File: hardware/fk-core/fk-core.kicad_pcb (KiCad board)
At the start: 2 copper layers, 0 parts

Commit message: MUP based board is the primary board now.
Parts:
- added C1: 18pF, RocketScreamKicadLibrary:CAP-0402, F.Cu at (139.2, 81.3)
- added C10: 4.7uF 10V X5R, RocketScreamKicadLibrary:CAP-0402, F.Cu at (139.4, 117.3)
- added C11: 4.7uF 10V X5R, RocketScreamKicadLibrary:CAP-0402, F.Cu at (139.4, 77.7)
- added C12: 100nF, RocketScreamKicadLibrary:CAP-0402, F.Cu at (139.4, 76.5)
- added C13: 100nF, RocketScreamKicadLibrary:CAP-0402, F.Cu at (132.6, 102.6)
- added C14: 4.7uF 10V X5R, RocketScreamKicadLibrary:CAP-0402, F.Cu at (133.7, 85.3)
- added C15: 1uF 10V X5R, RocketScreamKicadLibrary:CAP-0402, F.Cu at (139.2, 109.0)
- added C16: 4.7uF 10V X5R, RocketScreamKicadLibrary:CAP-0402, F.Cu at (136.4, 116.6)
- added C17: 4.7uF 10V X5R, RocketScreamKicadLibrary:CAP-0402, F.Cu at (137.7, 109.0)
- added C18: 4.7nF 25V X7R, RocketScreamKicadLibrary:CAP-0402, F.Cu at (145.8, 135.0)
- added C19: 1uF 10V X5R, RocketScreamKicadLibrary:CAP-0402, F.Cu at (140.0, 104.6)
- added C2: 18pF, RocketScreamKicadLibrary:CAP-0402, F.Cu at (141.2, 83.3)
- added C20: 1uF 10V X5R, RocketScreamKicadLibrary:CAP-0603, F.Cu at (143.1, 119.2)
- added C3: 100nF, RocketScreamKicadLibrary:CAP-0402, F.Cu at (145.0, 84.8)
- added C4: 100nF, RocketScreamKicadLibrary:CAP-0402, F.Cu at (132.5, 85.9)
- added C5: 1uF 10V X5R, RocketScreamKicadLibrary:CAP-0402, F.Cu at (146.3, 84.8)
- added C6: 100nF, RocketScreamKicadLibrary:CAP-0402, F.Cu at (135.0, 85.3)
- added C7: 100nF, RocketScreamKicadLibrary:CAP-0402, F.Cu at (147.3, 93.4)
- added C8: 100nF, RocketScreamKicadLibrary:CAP-0402, F.Cu at (131.6, 95.5)
- added C9: 1uF 50V X5R, RocketScreamKicadLibrary:CAP-0603, F.Cu at (134.1, 109.0)
- added D1: Orange, RocketScreamKicadLibrary:LED-0603, F.Cu at (144.5, 102.9)
- added D2: LED-DUAL, RocketScreamKicadLibrary:LED-1615, F.Cu at (144.5, 112.1)
- added D3: PRTR5V0U2X, RocketScreamKicadLibrary:SOT-143B, F.Cu at (148.0, 125.8)
- added D4: PMEG3020CPA, RocketScreamKicadLibrary:SOT-1016, F.Cu at (131.8, 110.7)
- added D5: Red, RocketScreamKicadLibrary:LED-0603, F.Cu at (131.4, 60.1)
- added F1: MF-PSMF050X-2, RocketScreamKicadLibrary:MF-PSMF020X, F.Cu at (138.2, 121.4)
- added G***: LOGO, logos:conservify_normal_3500, F.Cu at (134.1, 135.0)
- added G***: LOGO, logos:ngfk_normal_3500, F.Cu at (129.7, 139.8)
- added G***: LOGO, logos:osh_normal_3000, F.Cu at (137.8, 135.0)
- added J1: S2B-PH-SM4-TB, RocketScreamKicadLibrary:S2B-PH-SM4-TB, F.Cu at (131.6, 128.7)
- added J2: MICRO-USB, RocketScreamKicadLibrary:MICRO-USB, F.Cu at (149.9, 132.4)
- added J3: RF-SMA-EDGE, RocketScreamKicadLibrary:RF-SMA-EDGE, F.Cu at (129.0, 69.9)
- added J4: CONN-HDR-1x19, RocketScreamKicadLibrary:HDR_1x19_Pitch2.54mm_WithoutSilk, F.Cu at (128.3, 99.1)
- added J5: CONN-HDR-1x19, RocketScreamKicadLibrary:HDR_1x19_Pitch2.54mm_WithoutSilk, F.Cu at (151.1, 99.1)
- added J6: CONN-HDR-2x5, RocketScreamKicadLibrary:HDR_2x5_Pitch1.27mm, F.Cu at (145.0, 76.6)
- added J7: RF-SMA-EDGE, RocketScreamKicadLibrary:RF-SMA-EDGE, F.Cu at (143.8, 50.0)
- added L1: BKP1005TS121-T, RocketScreamKicadLibrary:IND-0402, F.Cu at (140.7, 117.3)
- added L2: BKP1005TS121-T, RocketScreamKicadLibrary:IND-0402, F.Cu at (131.2, 85.9)
- added M1: MOUNT_HOLE, RocketScreamKicadLibrary:HOLE_NPTH_2.2MM, F.Cu at (128.4, 151.6)
- added M2: MOUNT_HOLE, RocketScreamKicadLibrary:HOLE_NPTH_2.2MM, F.Cu at (151.2, 151.5)
- added M3: MOUNT_HOLE, RocketScreamKicadLibrary:HOLE_NPTH_2.2MM, F.Cu at (128.4, 49.4)
- added M4: MOUNT_HOLE, RocketScreamKicadLibrary:HOLE_NPTH_2.2MM, F.Cu at (151.2, 49.4)
- added M7: MICROSD, microsd:MICROSD, F.Cu at (132.5, 137.5)
- added P1: CONN-HDR-MODULE, fk-core-mini-ultra-pro:Socket_Strip_Straight_1x05_Pitch2.54mm, F.Cu at (151.1, 148.6)
- added Q1: 2N7002LT1G, RocketScreamKicadLibrary:SOT-23, F.Cu at (141.0, 101.3)
- added R1: 2K2, RocketScreamKicadLibrary:RES-0402, F.Cu at (144.5, 101.3)
- added R10: 2K2, RocketScreamKicadLibrary:RES-0402, F.Cu at (132.1, 115.6)
- added R11: 100K, RocketScreamKicadLibrary:RES-0402, F.Cu at (147.3, 91.2)
- added R12: 10K, RocketScreamKicadLibrary:RES-0402, F.Cu at (142.0, 112.8)
- added R13: 2K2, RocketScreamKicadLibrary:RES-0402, F.Cu at (142.0, 111.5)
- added R14: 1k, RocketScreamKicadLibrary:RES-0603, F.Cu at (141.3, 121.0)
- added R15: 180, RocketScreamKicadLibrary:RES-0603, F.Cu at (143.1, 122.8)
- added R16: 470R, RocketScreamKicadLibrary:RES-0603, F.Cu at (131.4, 56.5)
- added R17: 4.7K, RocketScreamKicadLibrary:RES-0603, F.Cu at (145.8, 114.8)
- added R18: 4.7K, RocketScreamKicadLibrary:RES-0603, F.Cu at (145.8, 116.5)
- added R2: 330R, RocketScreamKicadLibrary:RES-0402, F.Cu at (145.8, 80.0)
- added R3: 330R, RocketScreamKicadLibrary:RES-0402, F.Cu at (147.3, 89.9)
- added R4: 10K, RocketScreamKicadLibrary:RES-0402, F.Cu at (144.5, 80.0)
- added R5: 1M, RocketScreamKicadLibrary:RES-0402, F.Cu at (145.8, 136.5)
- added R6: 1K18, RocketScreamKicadLibrary:RES-0402, F.Cu at (135.9, 109.0)
- added R7: 46K4, RocketScreamKicadLibrary:RES-0402, F.Cu at (132.1, 113.0)
- added R8: 10K, RocketScreamKicadLibrary:RES-0402, F.Cu at (132.1, 116.8)
- added R9: 2K94, RocketScreamKicadLibrary:RES-0402, F.Cu at (132.1, 114.3)
- added SW1: SPNO, RocketScreamKicadLibrary:TS-018, F.Cu at (151.7, 54.9)
- added U1: ATSAMD21G18A-AU, RocketScreamKicadLibrary:TQFP-48_7x7mm_Pitch0.5mm, F.Cu at (139.7, 91.4)
- added U2: BQ24074RGTT, RocketScreamKicadLibrary:QFN-16_3x3mm, F.Cu at (137.0, 113.0)
- added U3: RFM95W, RocketScreamKicadLibrary:RFM9xW, B.Cu at (139.7, 87.6)
- added U4: MCP1700T-3302E/MB, RocketScreamKicadLibrary:SOT-89, F.Cu at (143.3, 107.4)
- added U5: S25FL116K0XMFI041, RocketScreamKicadLibrary:SOIC-8-N, F.Cu at (136.1, 102.6)
- added U6: MAX1704XX, Housings_DFN_QFN:DFN-8-1EP_2x2mm_Pitch0.5mm, F.Cu at (145.5, 120.9)
- added U7: FGPMMOPA6H, FGPMMOPA6H:FGPMMOPA6H, B.Cu at (141.8, 62.2)
- added Y1: FC-135, RocketScreamKicadLibrary:ABS07, F.Cu at (138.9, 83.6)
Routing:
- net 3V3: track 0.00 -> 210.9 mm, vias 0 -> 19
- net /MISO: track 0.00 -> 96.4 mm, vias 0 -> 3
- net /SCK: track 0.00 -> 82.3 mm, vias 0 -> 4
- net /MOSI: track 0.00 -> 81.6 mm, vias 0 -> 4
- net GND: track 0.00 -> 69.4 mm, vias 0 -> 43
- net /D13: track 0.00 -> 68.8 mm, vias 0 -> 2
- net /D1: track 0.00 -> 67.1 mm, vias 0 -> 1
- net /D0: track 0.00 -> 65.0 mm, vias 0 -> 1
- net /SCL: track 0.00 -> 60.2 mm, vias 0 -> 1
- net /SDA: track 0.00 -> 57.5 mm, vias 0 -> 1
- net VBAT: track 0.00 -> 54.9 mm
- net Net-(J2-Pad4): track 0.00 -> 45.5 mm
- net /USB-: track 0.00 -> 45.4 mm
- net /USB+: track 0.00 -> 44.8 mm
- net /A1: track 0.00 -> 40.9 mm, vias 0 -> 1
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- added copper zone on B.Cu, net 3V3
- added copper zone on F.Cu, net 3V3
- added copper zone on B.Cu, net 5V0
- added copper zone on F.Cu, net 5V0
- added copper zone on B.Cu, net GND
- added copper zone on F.Cu, net GND
- added copper zone on F.Cu, net VBAT
- added copper zone on B.Cu, net VBUS
- added copper zone on F.Cu, net VBUS
- added copper zone on F.Cu, net VEXT
- added copper zone on F.Cu, net VIN
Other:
- board outline added: 26.2 x 105.4 mm
- net class Default: trace_width 0.1524 -> 0.254; via_dia 0.6858 -> 0.5; via_drill 0.3302 -> 0.3
- net class RF-50Ohm added: clearance 0.254, trace_width 1.27, via_dia 0.5, via_drill 0.3
- rule pad_to_mask_clearance: 0.2 -> 0.1016
- rule trace_min: 0.1524 -> 0.19
- rule via_min_drill: 0.3302 -> 0.3
- rule via_min_size: 0.6858 -> 0.4
- board text added: "0"
- board text added: "1"
- board text added: "10"
- board text added: "11"
- board text added: "12"
- board text added: "13"
- board text added: "2"
- board text added: "3"
- board text added: "30"
- board text added: "31"
- board text added: "3V3"
- board text added: "4"
- board text added: "5"
- board text added: "5V"
- board text added: "6"
- board text added: "7"
- board text added: "8"
- board text added: "9"
- board text added: "A0"
- board text added: "A1"
- board text added: "A2"
- board text added: "A3"
- board text added: "A4"
- board text added: "A5"
- board text added: "AREF"
- board text added: "ATN"
- board text added: "BAT"
- board text added: "CHG"
- board text added: "GND"
- board text added: "LED-D13"
- board text added: "MISO"
- board text added: "MOSI"
- board text added: "PG"
- board text added: "PWM"
- board text added: "RST"
- board text added: "SCK"
- board text added: "SCL"
- board text added: "SDA"
- board text added: "SWD"
- board text added: "Serial"
- board text added: "Serial1"
- board text added: "VBUS"
- board text added: "VIN"
- board text added: "VIN:5-10.5V"
- board text added: "v0.1"

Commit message: Incorporating suggestions from Dave.
* SW1 is awfully close to the RF connection on U7. Can this slide south? Pins 15/15/17/18 are all no connect, having a switch close to that would be easier.
* If you move J7 to the other side of the board, then we won't need a via in the middle of the RF transmission line there.
* R16 is sized to bias A1 at about 3 mA. the default is to toggle on/off when it's locking, then go low when the system is locked. Bumping R16 to ~ 1Kohm will half the current, which might be enough for a high brightness LED.
Done! Thanks!

* Could J3 get flipped so that the RF path stays on the bottom, instead of running through a Via?
Done! I had to narrow and get creative with the A1 trace to route around this, hopefully that's ok.

* Vbackup on U7 might be worthwhile to hookup. the current consumption is pretty low (7 uA) and will let the GPS lock faster when power is applied.
I'll look into doing this. I'm just worried about getting VBAT over to that end of the board, haha.

* If you rotate C1/C2 180 degrees, you can ground both of them at the same via/Ground node.
Good call, where would you put the new via? There's a tight fit right there with the 3v3 to the radio and the edge of the bottom GND fill.

* J1 is an SMT part. Is there one available with through hole mounting pins so the connector doesn't rip off the board?
Good idea, I'll dig around and see if we can find one.

* The BQ24074 supports temp sensing on the battery pack, but the JST connector only has Batt+ and GND. Did you set the charging current on the low side?
* The RFM95 sits right underneath the 32kHz Clock crystal for the SAMD21. The 32kHz is a fairly strong oscillator (32kHz Square wave that goes 0 to 3.3V) and I'm worried that it will couple directly into the RF output of the RFM95 through the Power supply or directly radiated through the board. A 4 layer board with full ground planes would help significantly.

We based our board on an already designed and produced one and these a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
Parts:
- added M5, M6: FIDUCIAL, RocketScreamKicadLibrary:FIDUCIAL-1MM, F.Cu at (139.9, 163.3)
- J3, J7: moved to B.Cu
- R16: value 470R -> 1k
- moved SW1 16.3 mm to (151.7, 71.2)
- turned C1 to 135 degrees
- turned C2 to 315 degrees
- turned J7 to 270 degrees
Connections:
- U7 pad 4: (no net) -> VBAT
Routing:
- net VBAT: track 54.9 -> 114.1 mm, vias 0 -> 1
- net /RST: track 31.0 -> 14.7 mm
- net GND: track 69.4 -> 76.0 mm, vias 43 -> 45
- net /A1: track 40.9 -> 42.2 mm
- net Net-(C1-Pad2): track 6.68 -> 7.73 mm
- net Net-(C2-Pad2): track 5.61 -> 6.66 mm
- net 3V3: track 210.9 -> 209.9 mm, vias 19 -> 18
- net Net-(J3-Pad1): track 13.2 -> 13.7 mm, vias 1 -> 0
- net Net-(J7-Pad1): vias 2 -> 0

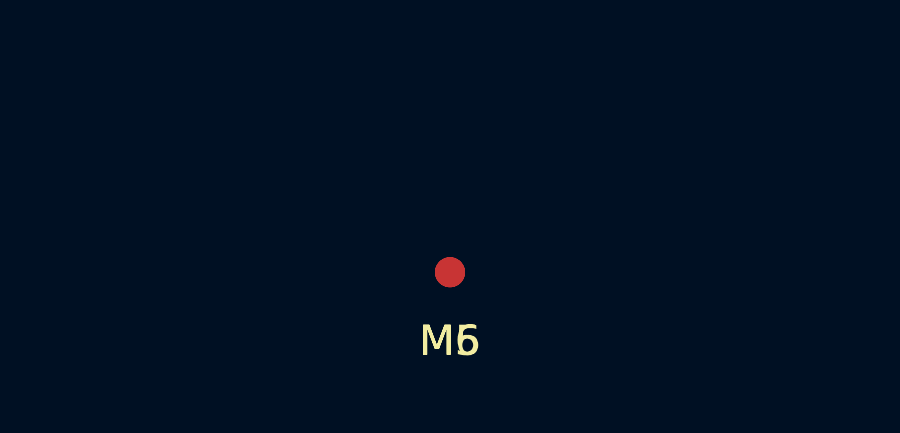
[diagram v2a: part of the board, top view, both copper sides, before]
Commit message: Remove fudicial for now.
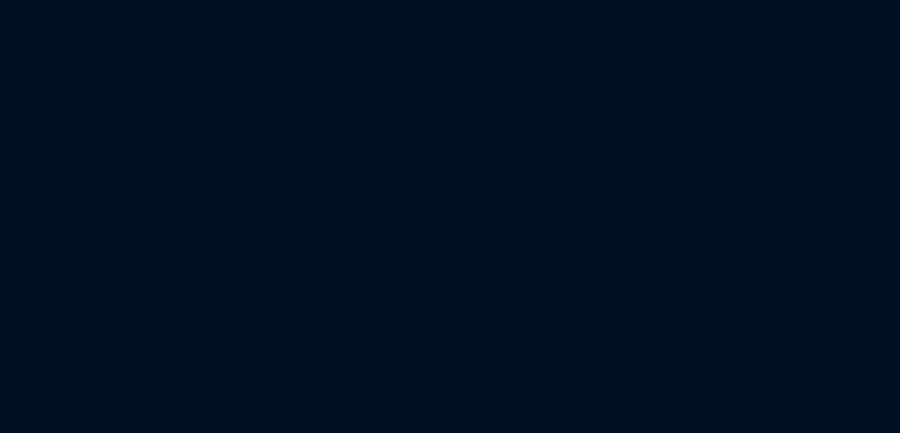
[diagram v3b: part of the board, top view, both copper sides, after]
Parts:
- removed M5, M6: FIDUCIAL, RocketScreamKicadLibrary:FIDUCIAL-1MM
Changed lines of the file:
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@@
   (general
     (links 220)
-    (no_connects 0)
-    (area 126.724999 47.724999 153.075001 153.275001)
+    (no_connects 77)
+    (area 104.521 44.198381 174.451 166.690001)
     (thickness 1.6)
     (drawings 86)
     (tracks 1006)
     (zones 0)
-    (modules 74)
+    (modules 72)
     (nets 68)
   )
@@
   )
   (setup
-    (last_trace_width 0.2032)
+    (last_trace_width 0.254)
     (user_trace_width 0.2032)
     (user_trace_width 0.254)
@@
       (xy 1.374306 0.851583) (xy 1.397389 0.846667) (xy 1.419502 0.853764)) (layer F.SilkS) (width 0.01))
   )
-  (module RocketScreamKicadLibrary:FIDUCIAL-1MM (layer F.Cu)
-    (at 139.9 163.275001)
-    (descr "Circular Fiducial, 1mm bare copper top; 2.54mm keepout")
-    (tags marker)
-    (attr virtual)
-    (fp_text reference M5 (at 0 2.286) (layer F.SilkS)
-      (effects (font (size 1 1) (thickness 0.15)))
-    )
-    (fp_text value FIDUCIAL (at 0 -2.032) (layer F.Fab)
-      (effects (font (size 1 1) (thickness 0.15)))
-    )
-    (pad ~ smd circle (at 0 0) (size 1 1) (layers F.Cu F.Mask)
-      (solder_mask_margin 0.5) (clearance 0.5))
-  )
-  (module RocketScreamKicadLibrary:FIDUCIAL-1MM (layer F.Cu)
-    (at 139.9 163.275001)
-    (descr "Circular Fiducial, 1mm bare copper top; 2.54mm keepout")
-    (tags marker)
-    (attr virtual)
-    (fp_text reference M6 (at 0 2.286) (layer F.SilkS)
-      (effects (font (size 1 1) (thickness 0.15)))
-    )
-    (fp_text value FIDUCIAL (at 0 -2.032) (layer F.Fab)
-      (effects (font (size 1 1) (thickness 0.15)))
-    )
-    (pad ~ smd circle (at 0 0) (size 1 1) (layers F.Cu F.Mask)
-      (solder_mask_margin 0.5) (clearance 0.5))
-  )
   (gr_text v0.1 (at 128.52 147.25) (layer F.SilkS)
     (effects (font (size 0.8 0.8) (thickness 0.15)))
@@
     (connect_pads (clearance 0.2032))
     (min_thickness 0.2032)
-    (fill (arc_segments 32) (thermal_gap 0.254) (thermal_bridge_width 0.254) (smoothing chamfer))
+    (fill yes (arc_segments 32) (thermal_gap 0.254) (thermal_bridge_width 0.254) (smoothing chamfer))
     (polygon
       (pts
@@
     (connect_pads (clearance 0.2032))
     (min_thickness 0.2032)
-    (fill (arc_segments 32) (thermal_gap 0.254) (thermal_bridge_width 0.254) (smoothing chamfer))
+    (fill yes (arc_segments 32) (thermal_gap 0.254) (thermal_bridge_width 0.254) (smoothing chamfer))
     (polygon
       (pts
@@
     (connect_pads (clearance 0.2032))
     (min_thickness 0.253)
-    (fill (arc_segments 32) (thermal_gap 0.254) (thermal_bridge_width 0.254) (smoothing chamfer))
+    (fill yes (arc_segments 32) (thermal_gap 0.254) (thermal_bridge_width 0.254) (smoothing chamfer))
     (polygon
       (pts
@@
     (connect_pads (clearance 0.2032))
     (min_thickness 0.2032)
-    (fill (arc_segments 32) (thermal_gap 0.254) (thermal_bridge_width 0.254) (smoothing chamfer))
+    (fill yes (arc_segments 32) (thermal_gap 0.254) (thermal_bridge_width 0.254) (smoothing chamfer))
     (polygon
       (pts
@@
     (connect_pads (clearance 0.2032))
     (min_thickness 0.253)
-    (fill (arc_segments 32) (thermal_gap 0.254) (thermal_bridge_width 0.254) (smoothing chamfer))
+    (fill yes (arc_segments 32) (thermal_gap 0.254) (thermal_bridge_width 0.254) (smoothing chamfer))
     (polygon
       (pts
@@
     (connect_pads (clearance 0.254))
     (min_thickness 0.253)
-    (fill (arc_segments 32) (thermal_gap 0.254) (thermal_bridge_width 0.254) (smoothing chamfer))
+    (fill yes (arc_segments 32) (thermal_gap 0.254) (thermal_bridge_width 0.254) (smoothing chamfer))
     (polygon
       (pts
@@
     (connect_pads (clearance 0.2032))
     (min_thickness 0.253)
-    (fill (arc_segments 32) (thermal_gap 0.254) (thermal_bridge_width 0.254) (smoothing chamfer))
+    (fill yes (arc_segments 32) (thermal_gap 0.254) (thermal_bridge_width 0.254) (smoothing chamfer))
     (polygon
       (pts
@@
     (connect_pads (clearance 0.2032))
     (min_thickness 0.253)
-    (fill (arc_segments 32) (thermal_gap 0.254) (thermal_bridge_width 0.254) (smoothing chamfer))
+    (fill yes (arc_segments 32) (thermal_gap 0.254) (thermal_bridge_width 0.254) (smoothing chamfer))
     (polygon
       (pts
@@
     (connect_pads (clearance 0.2032))
     (min_thickness 0.253)
-    (fill (arc_segments 32) (thermal_gap 0.254) (thermal_bridge_width 0.254) (smoothing chamfer))
+    (fill yes (arc_segments 32) (thermal_gap 0.254) (thermal_bridge_width 0.254) (smoothing chamfer))
     (polygon
       (pts
@@
     (connect_pads (clearance 0.2032))
     (min_thickness 0.253)
-    (fill (arc_segments 32) (thermal_gap 0.254) (thermal_bridge_width 0.254) (smoothing chamfer))
+    (fill yes (arc_segments 32) (thermal_gap 0.254) (thermal_bridge_width 0.254) (smoothing chamfer))
     (polygon
       (pts
@@
     (connect_pads (clearance 0.2032))
     (min_thickness 0.254)
-    (fill (arc_segments 16) (thermal_gap 0.508) (thermal_bridge_width 0.508))
+    (fill yes (arc_segments 16) (thermal_gap 0.508) (thermal_bridge_width 0.508))
     (polygon
       (pts
@@
     (connect_pads (clearance 0.2032))
     (min_thickness 0.254)
-    (fill (arc_segments 16) (thermal_gap 0.508) (thermal_bridge_width 0.508))
+    (fill yes (arc_segments 16) (thermal_gap 0.508) (thermal_bridge_width 0.508))
     (polygon
       (pts
@@
     (connect_pads (clearance 0.2032))
     (min_thickness 0.254)
-    (fill (arc_segments 16) (thermal_gap 0.508) (thermal_bridge_width 0.508))
+    (fill yes (arc_segments 16) (thermal_gap 0.508) (thermal_bridge_width 0.508))
     (polygon
       (pts
@@
     (connect_pads (clearance 0.2032))
     (min_thickness 0.254)
-    (fill (arc_segments 16) (thermal_gap 0.508) (thermal_bridge_width 0.508))
+    (fill yes (arc_segments 16) (thermal_gap 0.508) (thermal_bridge_width 0.508))
     (polygon
       (pts
@@
     (connect_pads (clearance 0.2032))
     (min_thickness 0.253)
-    (fill (arc_segments 32) (thermal_gap 0.254) (thermal_bridge_width 0.254) (smoothing chamfer))
+    (fill yes (arc_segments 32) (thermal_gap 0.254) (thermal_bridge_width 0.254) (smoothing chamfer))
     (polygon
       (pts
@@
     (connect_pads (clearance 0.2032))
     (min_thickness 0.254)
-    (fill (arc_segments 16) (thermal_gap 0.508) (thermal_bridge_width 0.508))
+    (fill yes (arc_segments 16) (thermal_gap 0.508) (thermal_bridge_width 0.508))
     (polygon
       (pts
@@
     (connect_pads (clearance 0.2032))
     (min_thickness 0.254)
-    (fill (arc_segments 16) (thermal_gap 0.508) (thermal_bridge_width 0.508))
+    (fill yes (arc_segments 16) (thermal_gap 0.508) (thermal_bridge_width 0.508))
     (polygon
       (pts
